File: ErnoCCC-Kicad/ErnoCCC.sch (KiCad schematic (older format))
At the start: 89 parts, among them J1 6VAC, J2 ICSP, J3 FTDI, J4 Erno Controller, J5 SWITCH, J6 LED OUT, Q1 BC847, Q2 BC847, Q3 BC847, SW1 SW_Push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

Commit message: Adding a D10 Breakout for later Vectrol (or MOSFET) experiments
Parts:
- added TP15: D10, TestPoint:TestPoint_THTPad_D1.5mm_Drill0.7mm, symbol Connector:TestPoint
- D1: symbol Diode_Bridge:HDS20M -> ErnoCCC-rescue:HDS20M-Diode_Bridge
- D7, D9: symbol Display_Character:OLED-128-64-I2C -> ErnoCCC-rescue:OLED-128-64-I2C-Display_Character
- U10, U9: symbol Relay_SolidState:CPC2317N -> ErnoCCC-rescue:CPC2317N-Relay_SolidState
- U11: symbol Driver_LED:AL8862SP-13 -> ErnoCCC-rescue:AL8862SP-13-Driver_LED
- U5: symbol Regulator_Linear:LD29150DT50R -> ErnoCCC-rescue:LD29150DT50R-Regulator_Linear
- U6, U7, U8: symbol Relay_SolidState:CPC2017N -> ErnoCCC-rescue:CPC2017N-Relay_SolidState
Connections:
- net labels added: D10
- wire segments 334 -> 335
- no-connect marks 3 -> 2
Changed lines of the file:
@@
 	2000 4700 2150 4700
 $Comp
-L Relay_SolidState:CPC2017N U6
+L ErnoCCC-rescue:CPC2017N-Relay_SolidState U6
 U 1 1 5E30DB67
 P 7950 3600
@@
 	8700 3300 8700 3400
 $Comp
-L Relay_SolidState:CPC2017N U7
+L ErnoCCC-rescue:CPC2017N-Relay_SolidState U7
 U 1 1 5E368DC6
 P 7950 4600
@@
 	8700 4300 8700 4400
 $Comp
-L Relay_SolidState:CPC2017N U8
+L ErnoCCC-rescue:CPC2017N-Relay_SolidState U8
 U 1 1 5E377C4B
 P 7950 5600
@@
 	8900 4700 8900 4300
 $Comp
-L Relay_SolidState:CPC2317N U10
+L ErnoCCC-rescue:CPC2317N-Relay_SolidState U10
 U 1 1 5E2947AB
 P 9400 4600
@@
 	9100 3500 9000 3500
 $Comp
-L Relay_SolidState:CPC2317N U9
+L ErnoCCC-rescue:CPC2317N-Relay_SolidState U9
 U 1 1 5E264720
 P 9400 3600
@@
 $EndComp
 $Comp
-L Diode_Bridge:HDS20M D1
+L ErnoCCC-rescue:HDS20M-Diode_Bridge D1
 U 1 1 5E4FFE7A
 P 1350 950
@@
 	5950 6150 5950 6300
 $Comp
-L Display_Character:OLED-128-64-I2C D7
+L ErnoCCC-rescue:OLED-128-64-I2C-Display_Character D7
 U 1 1 5E62B592
 P 3950 3850
@@
 Wire Wire Line
 	3500 3600 3550 3600
-NoConn ~ 2000 2600
 Wire Wire Line
 	1400 5100 1400 5200
@@
 	2000 2500 2150 2500
 $Comp
-L Driver_LED:AL8862SP-13 U11
+L ErnoCCC-rescue:AL8862SP-13-Driver_LED U11
 U 1 1 5E89662B
 P 8600 1850
@@
 Connection ~ 8850 5500
 $Comp
-L Display_Character:OLED-128-64-I2C D9
+L ErnoCCC-rescue:OLED-128-64-I2C-Display_Character D9
 U 1 1 5F3E6501
 P 3950 2900
@@
 	3500 2750 3550 2750
 $Comp
-L Regulator_Linear:LD29150DT50R U5
+L ErnoCCC-rescue:LD29150DT50R-Regulator_Linear U5
 U 1 1 5E4E1D57
 P 2850 950
@@
 Wire Wire Line
 	2850 1450 2850 1650
+Text Label 2150 2600 0    50   ~ 0
+D10
+$Comp
+L Connector:TestPoint TP15
+U 1 1 5E0E3D08
+P 2400 2600
+F 0 "TP15" V 2350 2800 50  0000 L CNN
+F 1 "D10" V 2350 2550 50  0000 L CNN
+F 2 "TestPoint:TestPoint_THTPad_D1.5mm_Drill0.7mm" H 2600 2600 50  0001 C CNN
+F 3 "~" H 2600 2600 50  0001 C CNN
+	1    2400 2600
+	0    1    1    0
+$EndComp
+Wire Wire Line
+	2000 2600 2400 2600
 $EndSCHEMATC

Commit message: Adding TPs to a Header, fixing disconnected GND planes
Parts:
- added J7: Conn_01x07, Connector_PinHeader_2.54mm:PinHeader_1x07_P2.54mm_Horizontal, symbol Connector_Generic:Conn_01x07
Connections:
- net labels added: GRAY-A, GRAY-B, POTA, POTB
- wire segments 335 -> 344
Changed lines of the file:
@@
 Text Label 4500 7100 0    50   ~ 0
 ICP1
-Wire Wire Line
-	4500 7000 4500 7100
 $Comp
 L Connector:TestPoint TP5
@@
 U 1 1 5E5035B9
 P 10300 3500
-F 0 "J4" H 10380 3542 50  0000 L CNN
+F 0 "J4" H 10250 3800 50  0000 L CNN
 F 1 "Erno Controller" H 10300 3150 50  0000 L CNN
 F 2 "TerminalBlock_Phoenix:TerminalBlock_Phoenix_MPT-0,5-5-2.54_1x05_P2.54mm_Horizontal" H 10300 3500 50  0001 C CNN
@@
 Wire Wire Line
 	2000 2600 2400 2600
+$Comp
+L Connector_Generic:Conn_01x07 J7
+U 1 1 5E107107
+P 5750 5100
+F 0 "J7" H 5668 4575 50  0000 C CNN
+F 1 "Conn_01x07" H 5668 4666 50  0000 C CNN
+F 2 "Connector_PinHeader_2.54mm:PinHeader_1x07_P2.54mm_Horizontal" H 5750 5100 50  0001 C CNN
+F 3 "~" H 5750 5100 50  0001 C CNN
+	1    5750 5100
+	-1   0    0    1
+$EndComp
+Text Label 6050 4800 0    50   ~ 0
+D10
+Text Label 6050 5200 0    50   ~ 0
+~STOP~
+Text Label 4500 7200 0    50   ~ 0
+GRAY-A
+Text Label 4500 6100 0    50   ~ 0
+GRAY-B
+Wire Wire Line
+	4450 6000 4450 6100
+Wire Wire Line
+	4450 6100 4500 6100
+Wire Wire Line
+	4500 7000 4500 7200
+Text Label 6050 5400 0    50   ~ 0
+GRAY-A
+Text Label 6050 5300 0    50   ~ 0
+GRAY-B
+Text Label 6050 5100 0    50   ~ 0
+SSR
+Text Label 8850 5350 0    50   ~ 0
+POTB
+Text Label 8700 4950 0    50   ~ 0
+POTA
+Text Label 6050 5000 0    50   ~ 0
+POTA
+Text Label 6050 4900 0    50   ~ 0
+POTB
+Wire Wire Line
+	5950 4800 6050 4800
+Wire Wire Line
+	5950 4900 6050 4900
+Wire Wire Line
+	5950 5000 6050 5000
+Wire Wire Line
+	5950 5100 6050 5100
+Wire Wire Line
+	5950 5200 6050 5200
+Wire Wire Line
+	5950 5300 6050 5300
+Wire Wire Line
+	5950 5400 6050 5400
 $EndSCHEMATC

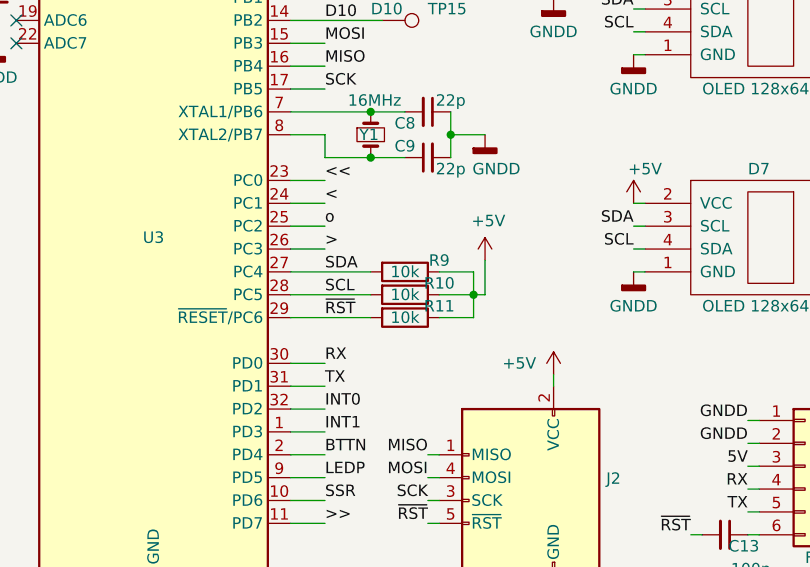
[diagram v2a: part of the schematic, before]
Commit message: Fixing I2C Pullups Rs, removing invalid Gerbers
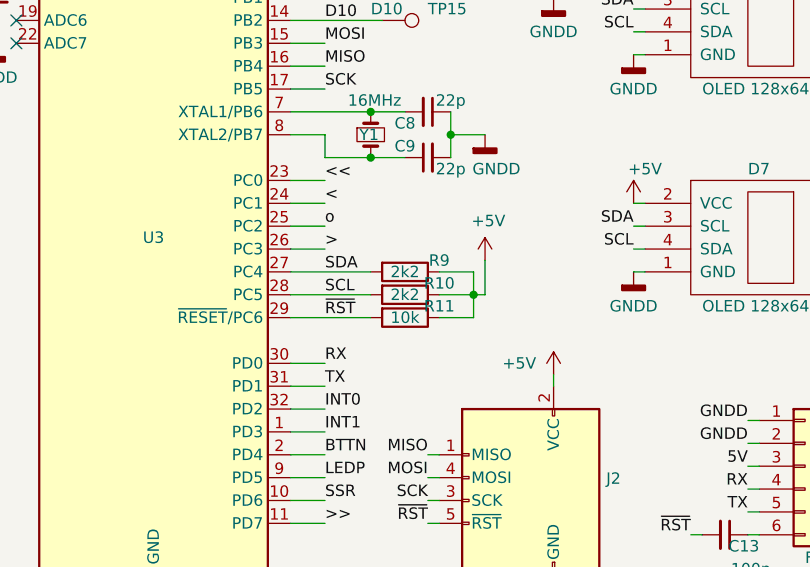
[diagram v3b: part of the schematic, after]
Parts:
- R10, R9: value 10k -> 2k2
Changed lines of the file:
@@
 P 2500 3700
 F 0 "R9" V 2450 3850 50  0000 C CNN
-F 1 "10k" V 2500 3700 50  0000 C CNN
+F 1 "2k2" V 2500 3700 50  0000 C CNN
 F 2 "Resistor_SMD:R_0805_2012Metric" V 2430 3700 50  0001 C CNN
 F 3 "~" H 2500 3700 50  0001 C CNN
@@
 P 2500 3800
 F 0 "R10" V 2450 3950 50  0000 C CNN
-F 1 "10k" V 2500 3800 50  0000 C CNN
+F 1 "2k2" V 2500 3800 50  0000 C CNN
 F 2 "Resistor_SMD:R_0805_2012Metric" V 2430 3800 50  0001 C CNN
 F 3 "~" H 2500 3800 50  0001 C CNN

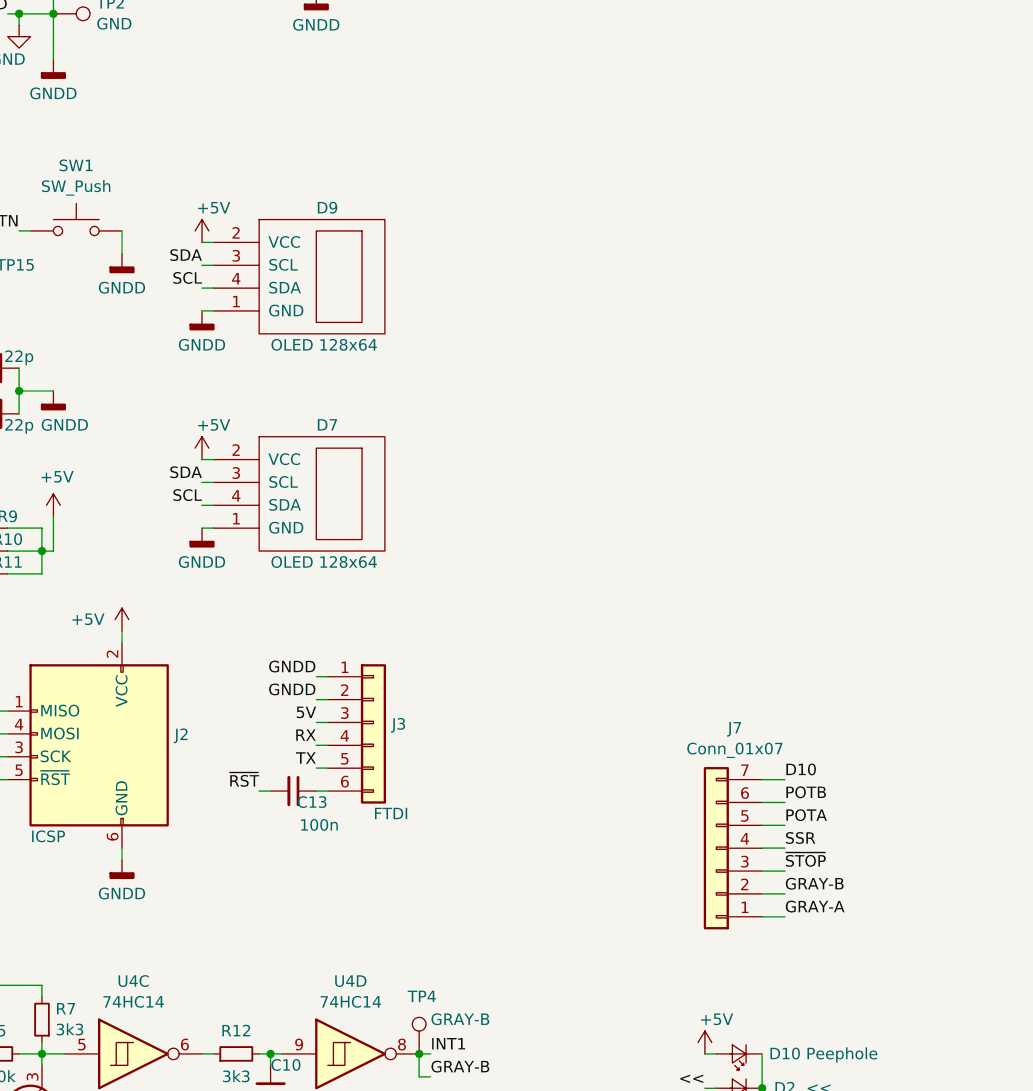
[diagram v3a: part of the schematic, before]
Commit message: Fixing i2c bus, making OLED polarity conifgurable, submitting final ReV gerbers
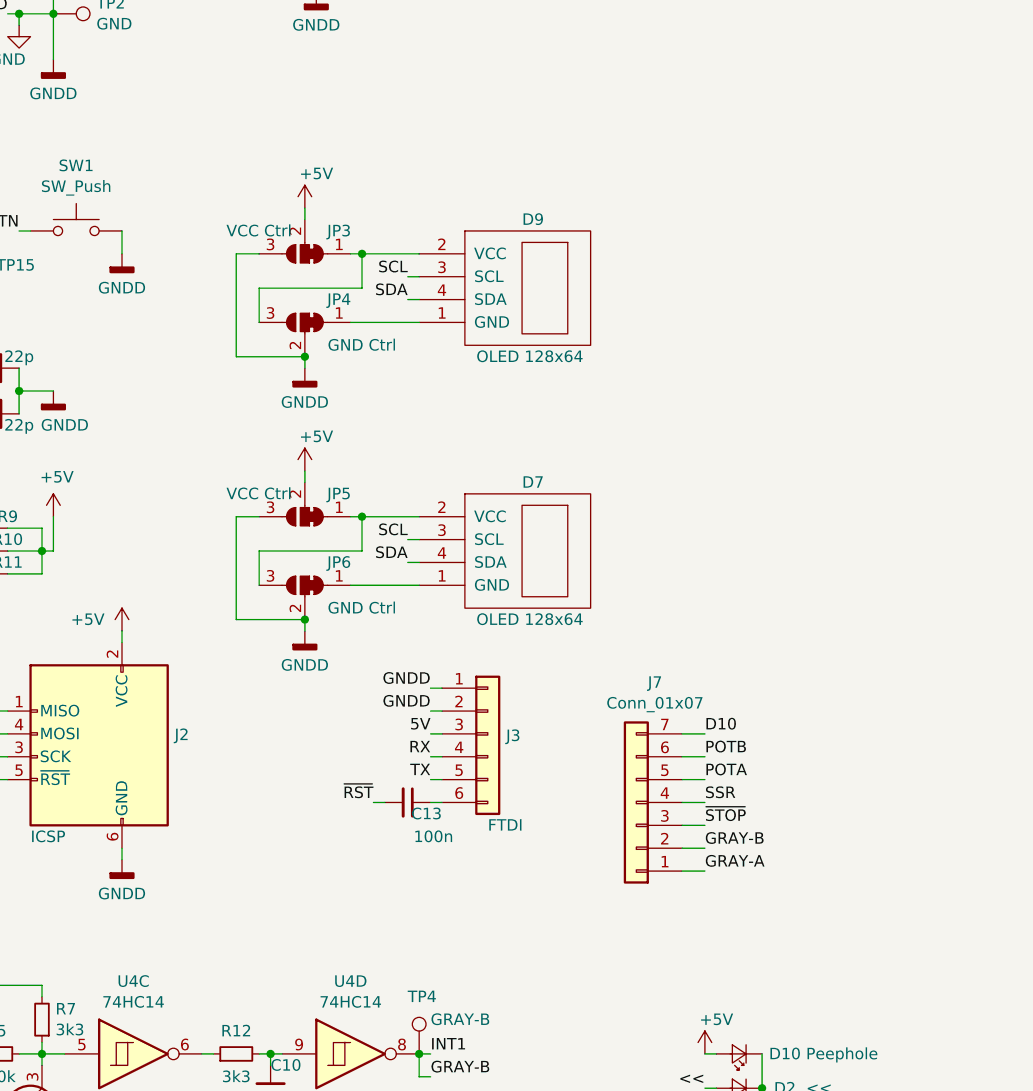
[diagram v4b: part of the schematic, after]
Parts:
- added JP3, JP5: VCC Ctrl, Jumper:SolderJumper-3_P1.3mm_Bridged12_RoundedPad1.0x1.5mm, symbol Jumper:SolderJumper_3_Bridged12
- added JP4, JP6: GND Ctrl, Jumper:SolderJumper-3_P1.3mm_Bridged12_RoundedPad1.0x1.5mm, symbol Jumper:SolderJumper_3_Bridged12
- JP2: footprint Jumper:SolderJumper-3_P1.3mm_Bridged12_Pad1.0x1.5mm -> Jumper:SolderJumper-3_P1.3mm_Bridged2Bar12_Pad1.0x1.5mm
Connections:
- wire segments 344 -> 362
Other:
- moved on the sheet: C13, D7, D9, J3, J7

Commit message: Schema Refactoring in progress...
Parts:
- removed R15, R16: 1k5, Resistor_SMD:R_0805_2012Metric, symbol Device:R_Small
- removed RV1, RV2, RV3, RV4, RV5: 4k7, Potentiometer_THT:Potentiometer_Bourns_3296W_Vertical, symbol Device:R_POT_Small
- removed TP12: ~STOP~, TestPoint:TestPoint_THTPad_D1.5mm_Drill0.7mm, symbol Connector:TestPoint
- removed TP13: PotA, TestPoint:TestPoint_THTPad_D1.5mm_Drill0.7mm, symbol Connector:TestPoint
- removed TP14: PotB, TestPoint:TestPoint_THTPad_D1.5mm_Drill0.7mm, symbol Connector:TestPoint
- removed U6, U7, U8: CPC2017N, ErnoCCC:SOIC-8, symbol ErnoCCC-rescue:CPC2017N-Relay_SolidState
- added C?: 100n, Capacitor_SMD:C_0805_2012Metric, symbol Device:C_Small
- added R?: 47k, Resistor_SMD:R_1210_3225Metric, symbol Device:R_Small
- added R?: 27k, Resistor_SMD:R_1210_3225Metric, symbol Device:R_Small
- added R?: 5k6, Resistor_SMD:R_1210_3225Metric, symbol Device:R_Small
- added RV?: 4k7, Potentiometer_THT:Potentiometer_Bourns_3296W_Vertical, symbol Device:R_POT_Small
- added U?: NCS20071, Package_TO_SOT_SMD:TSOT-23-5, symbol Amplifier_Operational:NCS20071
- added U?: CPC2317N, ErnoCCC:SOIC-8, symbol ErnoCCC-rescue:CPC2317N-Relay_SolidState
- J4: footprint TerminalBlock_Phoenix:TerminalBlock_Phoenix_MPT-0,5-5-2.54_1x05_P2.54mm_Horizontal -> TerminalBlock_Phoenix:TerminalBlock_Phoenix_MPT-0,5-7-2.54_1x07_P2.54mm_Horizontal; symbol Connector:Screw_Terminal_01x05 -> Connector:Screw_Terminal_01x07
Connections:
- net labels added: +15V, DAC, VCTRL
- wire segments 362 -> 324
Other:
- note added: "+15 VDC"
- note added: "GND"
- note added: "Green (PCB)"
- note added: "Green (Pot)"
- note removed: "Green"
- note removed: "Orange (Pot)"
- moved on the sheet: Q3, R18

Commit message: preparing for rev b
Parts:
- removed U?: CPC2317N, ErnoCCC:SOIC-8, symbol ErnoCCC-rescue:CPC2317N-Relay_SolidState
- R17: value 330 -> 470
- U?: symbol Amplifier_Operational:NCS20071 -> ErnoCCC-rescue:NCS20071-Amplifier_Operational
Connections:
- wire segments 324 -> 312
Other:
- moved on the sheet: TP10, TP11, TP6, TP7, TP8, TP9
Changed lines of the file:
@@
 $EndComp
-Wire Wire Line
-	9750 4500 9750 4700
-Connection ~ 9750 3500
 Wire Wire Line
 	9750 3400 9750 3500
-Wire Wire Line
-	9750 3500 9750 3700
 Wire Wire Line
 	9000 3900 9000 4500
 Connection ~ 9000 4500
-Connection ~ 9000 4900
-$Comp
-L power:GNDD #PWR022
-U 1 1 5E2947D3
-P 9000 6250
-F 0 "#PWR022" H 9000 6000 50  0001 C CNN
-F 1 "GNDD" H 9000 6100 50  0000 C CNN
-F 2 "" H 9000 6250 50  0001 C CNN
-F 3 "" H 9000 6250 50  0001 C CNN
-	1    9000 6250
-	1    0    0    -1
-$EndComp
-Wire Wire Line
-	9750 4700 9700 4700
-Wire Wire Line
-	9700 4500 9750 4500
 Wire Wire Line
 	8900 4700 9100 4700
@@
 	9100 4500 9000 4500
 Connection ~ 9000 3900
-Wire Wire Line
-	9750 3700 9700 3700
 Wire Wire Line
 	9700 3500 9750 3500
@@
 	1    0    0    -1
 $EndComp
-Wire Wire Line
-	9700 3900 9800 3900
-Wire Wire Line
-	9800 3900 9800 4050
 Text Notes 10400 3450 0    50   ~ 0
 Blue (PCB)
@@
 Text Notes 10400 3350 0    50   ~ 0
 Blue (Pot)
-Text Label 7300 3300 2    50   ~ 0
+Text Label 8150 3150 2    50   ~ 0
 <<
-Text Label 7300 3700 2    50   ~ 0
+Text Label 8150 3550 2    50   ~ 0
 <
-Text Label 7300 4300 2    50   ~ 0
+Text Label 8150 4150 2    50   ~ 0
 o
-Text Label 7300 4700 2    50   ~ 0
+Text Label 8150 4550 2    50   ~ 0
 >
-Text Label 7300 5300 2    50   ~ 0
+Text Label 8150 5150 2    50   ~ 0
 >>
 Wire Wire Line
 	8900 3250 8900 3300
-$Comp
-L Device:R_Small R17
-U 1 1 5E2DB41B
-P 8900 3150
-F 0 "R17" H 8841 3104 50  0000 R CNN
-F 1 "330" H 8841 3195 50  0000 R CNN
-F 2 "Resistor_SMD:R_0805_2012Metric" H 8900 3150 50  0001 C CNN
-F 3 "~" H 8900 3150 50  0001 C CNN
-	1    8900 3150
-	-1   0    0    1
-$EndComp
-Text Label 8850 3000 2    50   ~ 0
-SSR
 Wire Wire Line
 	8900 3000 8900 3050
@@
 L Connector:TestPoint TP8
 U 1 1 5E56BF42
-P 7450 3700
-F 0 "TP8" H 7250 3850 50  0000 L CNN
-F 1 "<" H 7400 3650 50  0000 L CNN
-F 2 "TestPoint:TestPoint_THTPad_D1.5mm_Drill0.7mm" H 7650 3700 50  0001 C CNN
-F 3 "~" H 7650 3700 50  0001 C CNN
-	1    7450 3700
+P 8300 3550
+F 0 "TP8" H 8100 3700 50  0000 L CNN
+F 1 "<" H 8250 3500 50  0000 L CNN
+F 2 "TestPoint:TestPoint_THTPad_D1.5mm_Drill0.7mm" H 8500 3550 50  0001 C CNN
+F 3 "~" H 8500 3550 50  0001 C CNN
+	1    8300 3550
 	1    0    0    -1
 $EndComp
@@
 L Connector:TestPoint TP7
 U 1 1 5E570475
-P 7450 3300
-F 0 "TP7" H 7250 3450 50  0000 L CNN
-F 1 "<<" H 7400 3250 50  0000 L CNN
-F 2 "TestPoint:TestPoint_THTPad_D1.5mm_Drill0.7mm" H 7650 3300 50  0001 C CNN
-F 3 "~" H 7650 3300 50  0001 C CNN
-	1    7450 3300
+P 8300 3150
+F 0 "TP7" H 8100 3300 50  0000 L CNN
+F 1 "<<" H 8250 3100 50  0000 L CNN
+F 2 "TestPoint:TestPoint_THTPad_D1.5mm_Drill0.7mm" H 8500 3150 50  0001 C CNN
+F 3 "~" H 8500 3150 50  0001 C CNN
+	1    8300 3150
 	1    0    0    -1
 $EndComp
@@
 L Connector:TestPoint TP9
 U 1 1 5E570F18
-P 7450 4300
-F 0 "TP9" H 7250 4450 50  0000 L CNN
-F 1 "o" H 7400 4250 50  0000 L CNN
-F 2 "TestPoint:TestPoint_THTPad_D1.5mm_Drill0.7mm" H 7650 4300 50  0001 C CNN
-F 3 "~" H 7650 4300 50  0001 C CNN
-	1    7450 4300
+P 8300 4150
+F 0 "TP9" H 8100 4300 50  0000 L CNN
+F 1 "o" H 8250 4100 50  0000 L CNN
+F 2 "TestPoint:TestPoint_THTPad_D1.5mm_Drill0.7mm" H 8500 4150 50  0001 C CNN
+F 3 "~" H 8500 4150 50  0001 C CNN
+	1    8300 4150
 	1    0    0    -1
 $EndComp
@@
 L Connector:TestPoint TP10
 U 1 1 5E5713A7
-P 7450 4700
-F 0 "TP10" H 7200 4850 50  0000 L CNN
-F 1 ">" H 7400 4650 50  0000 L CNN
-F 2 "TestPoint:TestPoint_THTPad_D1.5mm_Drill0.7mm" H 7650 4700 50  0001 C CNN
-F 3 "~" H 7650 4700 50  0001 C CNN
-	1    7450 4700
+P 8300 4550
+F 0 "TP10" H 8050 4700 50  0000 L CNN
+F 1 ">" H 8250 4500 50  0000 L CNN
+F 2 "TestPoint:TestPoint_THTPad_D1.5mm_Drill0.7mm" H 8500 4550 50  0001 C CNN
+F 3 "~" H 8500 4550 50  0001 C CNN
+	1    8300 4550
 	1    0    0    -1
 $EndComp
@@
 L Connector:TestPoint TP11
 U 1 1 5E571752
-P 7450 5300
-F 0 "TP11" H 7200 5450 50  0000 L CNN
-F 1 ">>" H 7400 5250 50  0000 L CNN
-F 2 "TestPoint:TestPoint_THTPad_D1.5mm_Drill0.7mm" H 7650 5300 50  0001 C CNN
-F 3 "~" H 7650 5300 50  0001 C CNN
-	1    7450 5300
+P 8300 5150
+F 0 "TP11" H 8050 5300 50  0000 L CNN
+F 1 ">>" H 8250 5100 50  0000 L CNN
+F 2 "TestPoint:TestPoint_THTPad_D1.5mm_Drill0.7mm" H 8500 5150 50  0001 C CNN
+F 3 "~" H 8500 5150 50  0001 C CNN
+	1    8300 5150
 	1    0    0    -1
 $EndComp
@@
 L Connector:TestPoint TP6
 U 1 1 5E571A52
-P 7450 3000
-F 0 "TP6" H 7250 3150 50  0000 L CNN
-F 1 "SSR" H 7400 2950 50  0000 L CNN
-F 2 "TestPoint:TestPoint_THTPad_D1.5mm_Drill0.7mm" H 7650 3000 50  0001 C CNN
-F 3 "~" H 7650 3000 50  0001 C CNN
-	1    7450 3000
-	1    0    0    -1
-$EndComp
-Wire Wire Line
-	7300 3000 7450 3000
-Wire Wire Line
-	7300 3300 7450 3300
-Wire Wire Line
-	7300 3700 7450 3700
-Wire Wire Line
-	7300 4300 7450 4300
-Wire Wire Line
-	7300 4700 7450 4700
-Wire Wire Line
-	7300 5300 7450 5300
+P 8300 2850
+F 0 "TP6" H 8100 3000 50  0000 L CNN
+F 1 "SSR" H 8250 2800 50  0000 L CNN
+F 2 "TestPoint:TestPoint_THTPad_D1.5mm_Drill0.7mm" H 8500 2850 50  0001 C CNN
+F 3 "~" H 8500 2850 50  0001 C CNN
+	1    8300 2850
+	1    0    0    -1
+$EndComp
+Wire Wire Line
+	8150 2850 8300 2850
+Wire Wire Line
+	8150 3150 8300 3150
+Wire Wire Line
+	8150 3550 8300 3550
+Wire Wire Line
+	8150 4150 8300 4150
+Wire Wire Line
+	8150 4550 8300 4550
+Wire Wire Line
+	8150 5150 8300 5150
 $Comp
 L 74xx:74HC14 U4
@@
 Wire Wire Line
 	9700 4300 9950 4300
-Wire Wire Line
-	9750 4500 10050 4500
-Connection ~ 9750 4500
 $Comp
 L Device:CP_Small C12
@@
 	4400 3850 4450 3850
 $Comp
-L Amplifier_Operational:NCS20071 U?
+L ErnoCCC-rescue:NCS20071-Amplifier_Operational U?
 U 1 1 5E204FD7
 P 6100 1150
@@
 	0    1    -1   0
 $EndComp
-$Comp
-L ErnoCCC-rescue:CPC2317N-Relay_SolidState U?
-U 1 1 5E570A7B
-P 9400 5650
-F 0 "U?" H 9400 5650 50  0000 C CNN
-F 1 "CPC2317N" H 9400 6100 50  0000 C CNN
-F 2 "ErnoCCC:SOIC-8" H 9400 5125 50  0001 C CIN
-F 3 "https://www.mouser.de/datasheet/2/240/CPC2317N-1548245.pdf" H 9400 5850 50  0001 L CNN
-	1    9400 5650
-	1    0    0    -1
-$EndComp
 Wire Wire Line
 	9950 4300 9950 3600
@@
 Wire Wire Line
 	10150 3500 9850 3500
-Wire Wire Line
-	9850 5750 9700 5750
-Wire Wire Line
-	9850 3500 9850 5750
-Text Label 9750 5950 0    50   ~ 0
-VCTRL
-Wire Wire Line
-	9700 5950 9750 5950
-Wire Wire Line
-	9000 4900 9000 5550
-Wire Wire Line
-	9100 5550 9000 5550
-Connection ~ 9000 5550
-Wire Wire Line
-	9000 5550 9000 5950
-Wire Wire Line
-	9100 5950 9000 5950
-Connection ~ 9000 5950
-Wire Wire Line
-	9000 5950 9000 6250
-Wire Wire Line
-	8900 4700 8900 5350
-Wire Wire Line
-	8900 5350 9100 5350
-Connection ~ 8900 4700
-Wire Wire Line
-	8900 5350 8900 5750
-Wire Wire Line
-	8900 5750 9100 5750
-Connection ~ 8900 5350
 Text Label 6750 1150 0    50   ~ 0
 VCTRL
-Wire Wire Line
-	8850 3000 8900 3000
 $Comp
 L power:GNDD #PWR?
@@
 Wire Wire Line
 	5500 1050 5550 1050
+Wire Wire Line
+	9700 4500 10050 4500
+Wire Wire Line
+	9850 3500 9850 3700
+Wire Wire Line
+	9850 3700 9700 3700
+Wire Wire Line
+	9700 3900 9750 3900
+Wire Wire Line
+	9750 3900 9750 4050
+Wire Wire Line
+	9750 4050 8700 4050
+Wire Wire Line
+	8850 3000 8900 3000
+Text Label 8850 3000 2    50   ~ 0
+SSR
+$Comp
+L Device:R_Small R17
+U 1 1 5E2DB41B
+P 8900 3150
+F 0 "R17" H 8841 3104 50  0000 R CNN
+F 1 "470" H 8841 3195 50  0000 R CNN
+F 2 "Resistor_SMD:R_0805_2012Metric" H 8900 3150 50  0001 C CNN
+F 3 "~" H 8900 3150 50  0001 C CNN
+	1    8900 3150
+	-1   0    0    1
+$EndComp
+Wire Wire Line
+	9700 5950 9750 5950
+Text Label 9750 5950 0    50   ~ 0
+VCTRL
+$Comp
+L power:GNDD #PWR022
+U 1 1 5E2947D3
+P 9000 5000
+F 0 "#PWR022" H 9000 4750 50  0001 C CNN
+F 1 "GNDD" H 9000 4850 50  0000 C CNN
+F 2 "" H 9000 5000 50  0001 C CNN
+F 3 "" H 9000 5000 50  0001 C CNN
+	1    9000 5000
+	1    0    0    -1
+$EndComp
+Text Label 8700 4050 2    50   ~ 0
+VCTRL
+Wire Wire Line
+	9000 4900 9000 5000
+Connection ~ 9000 4900
 $EndSCHEMATC
